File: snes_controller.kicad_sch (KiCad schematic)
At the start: 2 parts, among them J401 Conn_01x07, J402 Conn_01x07

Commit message: update title block
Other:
- company: (none) -> Butler Electronics
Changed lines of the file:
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@@
 (kicad_sch (version 20230121) (generator eeschema)
   (paper "A4")
+  (title_block
+    (date "2024-01-01")
+    (rev "A")
+    (company "Butler Electronics")
+    (comment 1 "Joshua Butler, MD, MHI")
+  )
   (no_connect (at 45.72 55.88))
   (no_connect (at 74.93 53.34))

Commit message: change footprint
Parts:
- J401, J402: footprint User_Footprint:SNES_Controller_Port -> User_Footprint:SNES_Controller_Port_Horizontal
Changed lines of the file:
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@@
       (effects (font (size 1.27 1.27)) hide)
     )
-    (property "Footprint" "User_Footprint:SNES_Controller_Port" (at 69.85 50.8 0)
+    (property "Footprint" "User_Footprint:SNES_Controller_Port_Horizontal" (at 69.85 50.8 0)
       (effects (font (size 1.27 1.27)) hide)
     )
@@
       (effects (font (size 1.27 1.27)) hide)
     )
-    (property "Footprint" "User_Footprint:SNES_Controller_Port" (at 40.64 50.8 0)
+    (property "Footprint" "User_Footprint:SNES_Controller_Port_Horizontal" (at 40.64 50.8 0)
       (effects (font (size 1.27 1.27)) hide)
     )

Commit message: update BOM
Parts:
- J401, J402: now left out of the parts list
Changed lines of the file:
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@@
   )
   (symbol (lib_id "Connector_Generic:Conn_01x07") (at 69.85 50.8 0) (mirror y) (unit 1)
-    (in_bom yes) (on_board yes) (dnp no) (fields_autoplaced)
+    (in_bom no) (on_board yes) (dnp no) (fields_autoplaced)
     (property "Reference" "J402" (at 69.85 39.37 0)
       (effects (font (size 1.27 1.27)))
@@
     )
     (property "Datasheet" "~" (at 69.85 50.8 0)
+      (effects (font (size 1.27 1.27)) hide)
+    )
+    (property "LCSC" "" (at 69.85 50.8 0)
+      (effects (font (size 1.27 1.27)) hide)
+    )
+    (property "Mouser" "" (at 69.85 50.8 0)
       (effects (font (size 1.27 1.27)) hide)
     )
@@
   )
   (symbol (lib_id "Connector_Generic:Conn_01x07") (at 40.64 50.8 0) (mirror y) (unit 1)
-    (in_bom yes) (on_board yes) (dnp no) (fields_autoplaced)
+    (in_bom no) (on_board yes) (dnp no) (fields_autoplaced)
     (property "Reference" "J401" (at 40.64 39.37 0)
       (effects (font (size 1.27 1.27)))
@@
       (effects (font (size 1.27 1.27)) hide)
     )
+    (property "LCSC" "" (at 40.64 50.8 0)
+      (effects (font (size 1.27 1.27)) hide)
+    )
+    (property "Mouser" "" (at 40.64 50.8 0)
+      (effects (font (size 1.27 1.27)) hide)
+    )

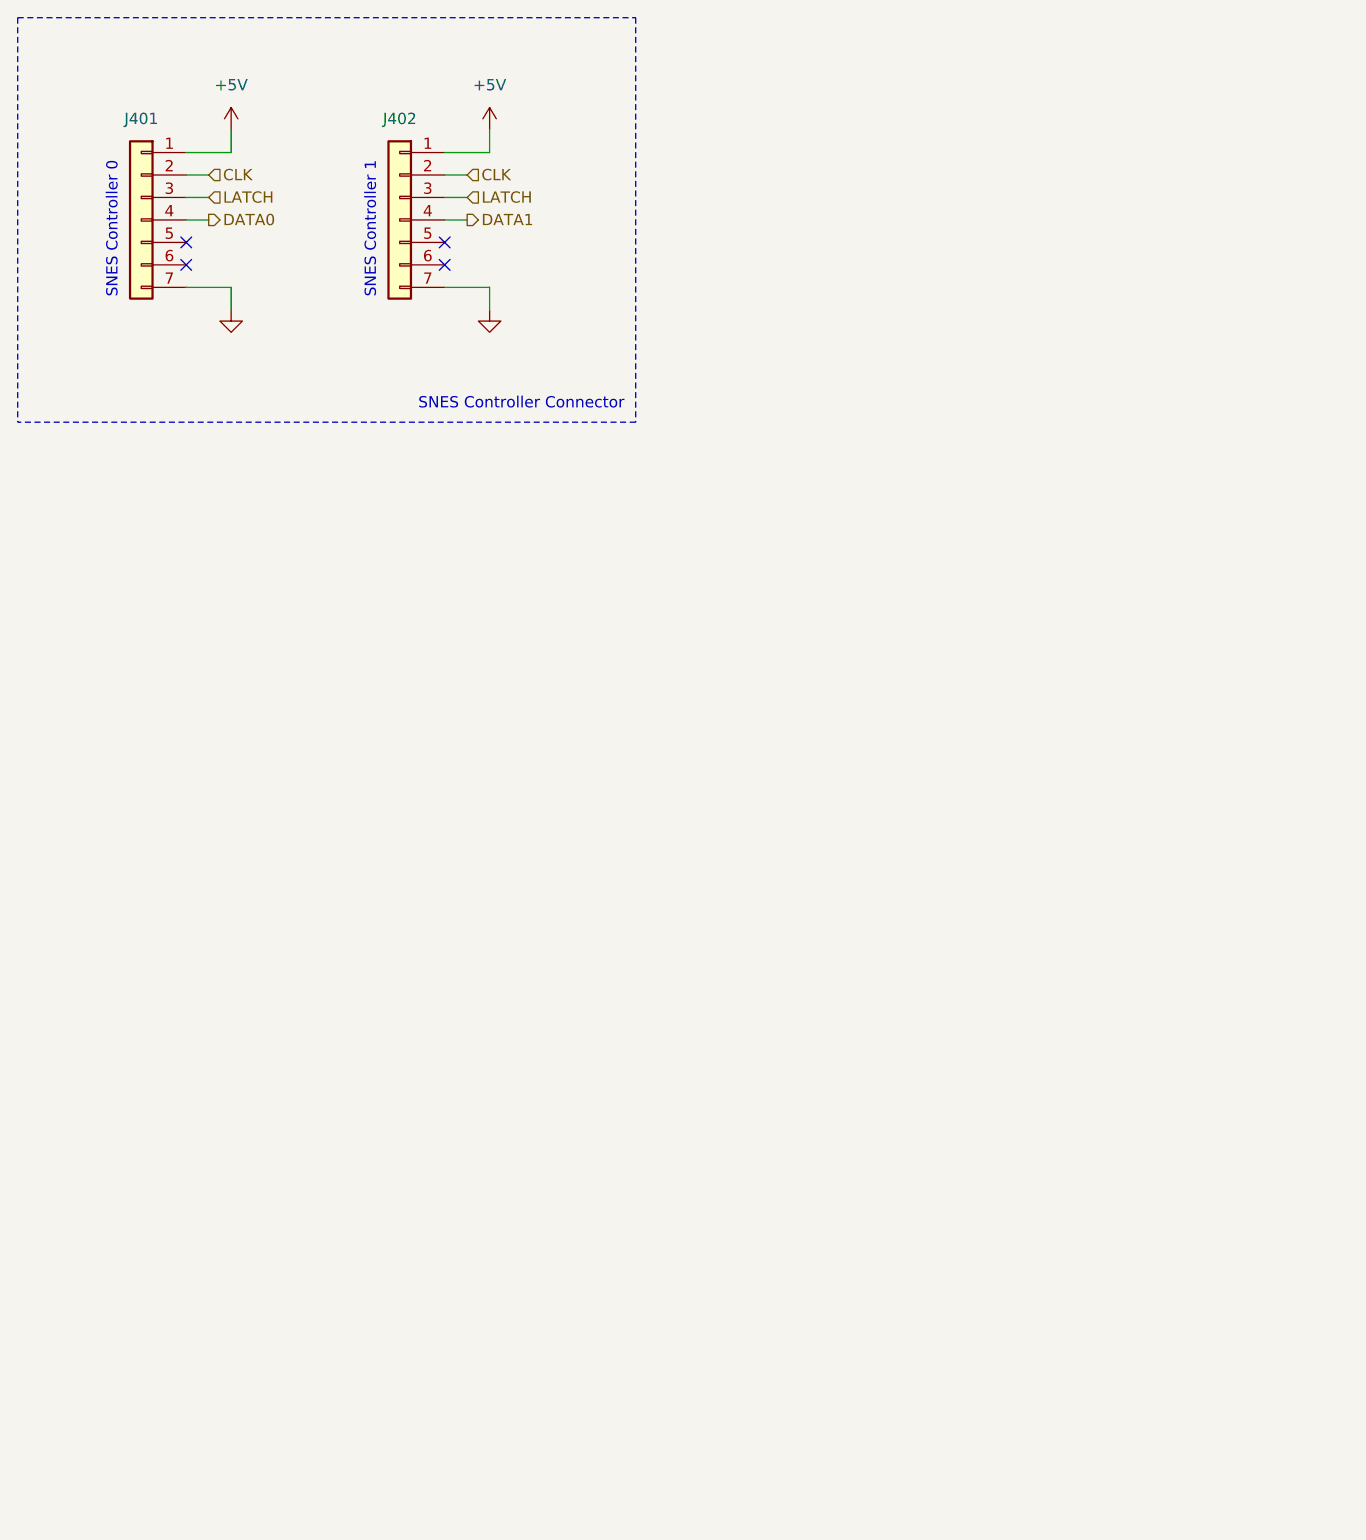
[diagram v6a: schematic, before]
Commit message: update schematic and pcb design to rev-b
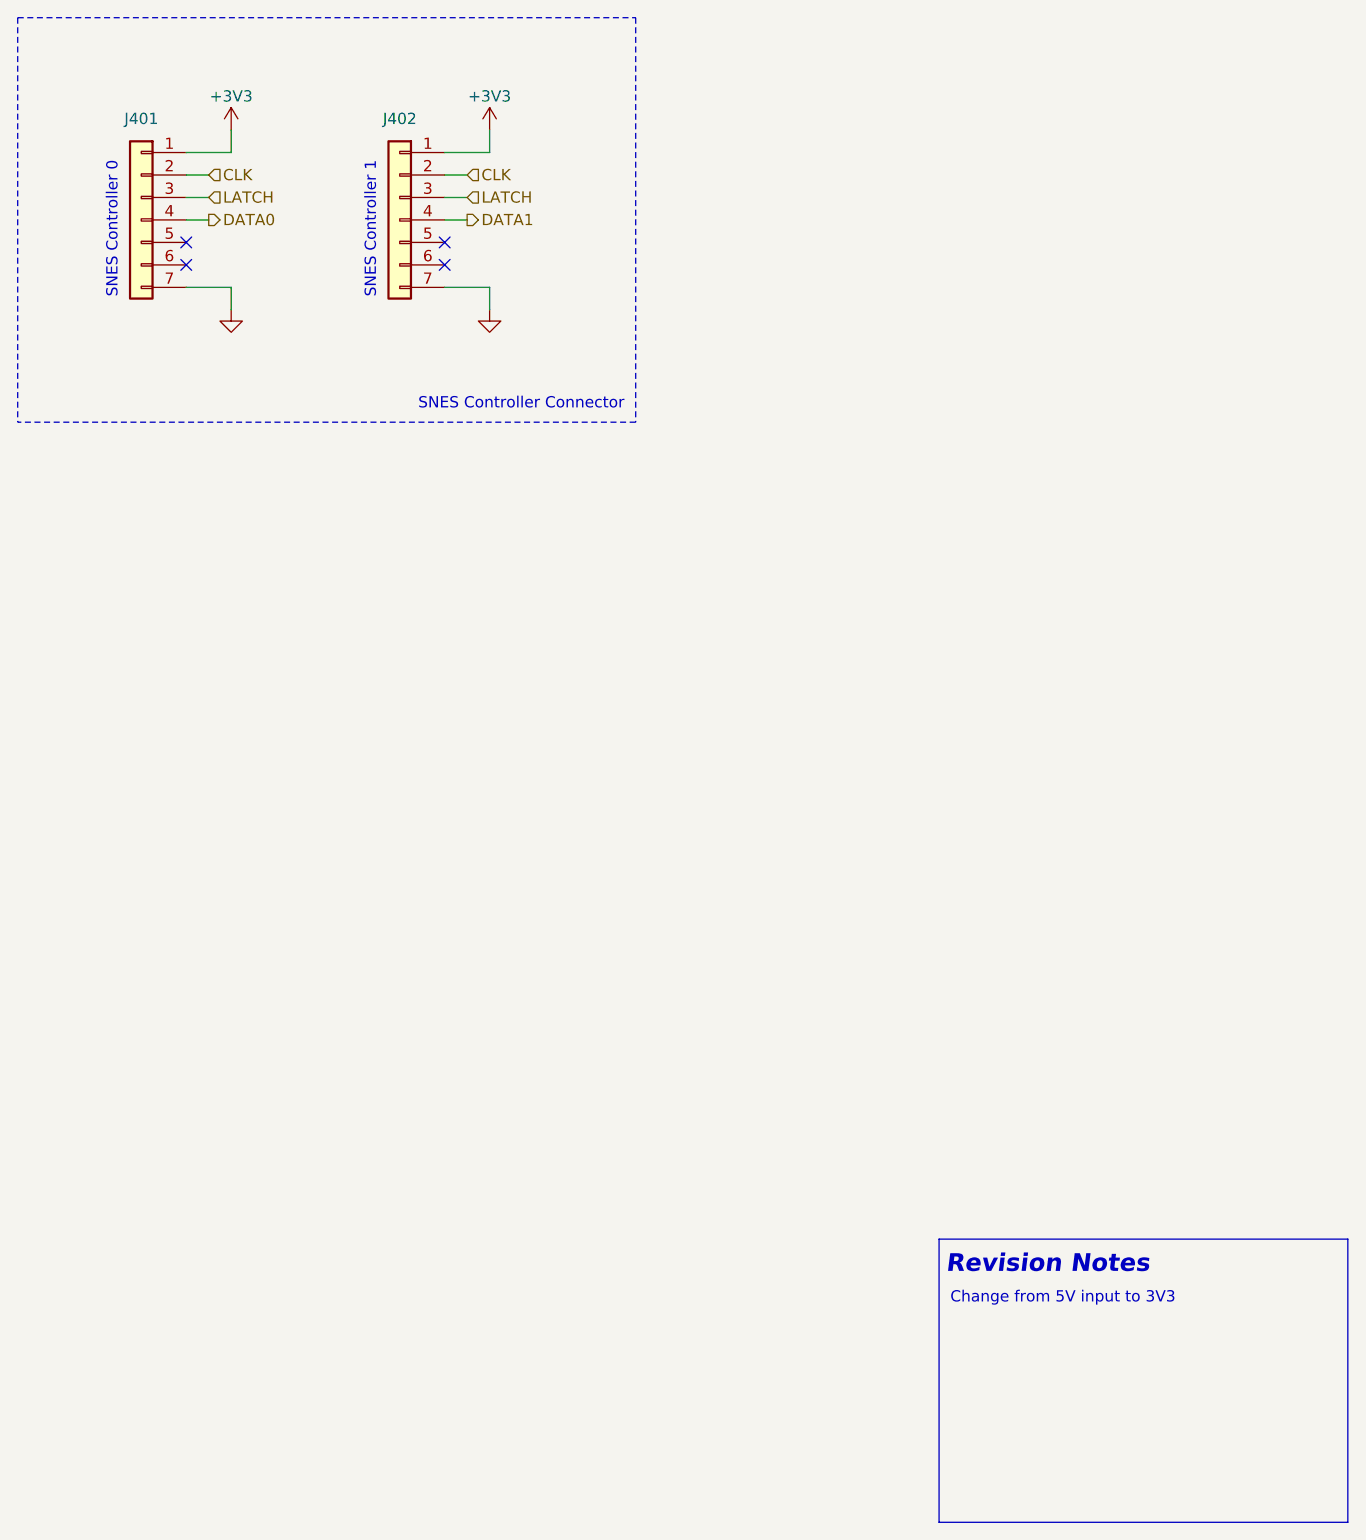
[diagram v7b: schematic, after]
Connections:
- net +5V renamed +3V3
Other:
- note added: "Change from 5V input to 3V3"
- note added: "Revision Notes"
